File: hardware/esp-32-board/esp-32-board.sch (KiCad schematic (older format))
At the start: 12 parts, among them J1 MainConnector, J2 Conn_01x06, J3 ESP-PROG-Program, J4 ESP-PROG-Debug, SW1 SW_Push, SW2 SW_Push, U1 ESP32-WROOM-32

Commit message: Reannotate schematic
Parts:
- renumbered C3 to C2, C4 to C3, C2 to C4, J3 to J1, J1 to J2, J4 to J3, J2 to J4
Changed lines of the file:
@@
 $EndComp
 $Comp
-L Device:C C3
+L Device:C C2
 U 1 1 5FAC9D96
 P 4850 2950
-F 0 "C3" V 4700 3000 50  0000 L CNN
+F 0 "C2" V 4700 3000 50  0000 L CNN
 F 1 "100nF" V 4700 2650 50  0000 L CNN
 F 2 "Capacitor_SMD:C_0805_2012Metric_Pad1.18x1.45mm_HandSolder" H 4888 2800 50  0001 C CNN
@@
 $EndComp
 $Comp
-L Device:C C4
+L Device:C C3
 U 1 1 5FACA76A
 P 4850 4250
-F 0 "C4" V 4700 4300 50  0000 L CNN
+F 0 "C3" V 4700 4300 50  0000 L CNN
 F 1 "100nF" V 4700 3950 50  0000 L CNN
 F 2 "Capacitor_SMD:C_0805_2012Metric_Pad1.18x1.45mm_HandSolder" H 4888 4100 50  0001 C CNN
@@
 $EndComp
 $Comp
-L Device:C C2
+L Device:C C4
 U 1 1 5FACAC23
 P 5000 1550
-F 0 "C2" H 5050 1650 50  0000 L CNN
+F 0 "C4" H 5050 1650 50  0000 L CNN
 F 1 "100nF" H 5100 1450 50  0000 L CNN
 F 2 "Capacitor_SMD:C_0805_2012Metric_Pad1.18x1.45mm_HandSolder" H 5038 1400 50  0001 C CNN
@@
 	7400 2400 6850 2400
 $Comp
-L Connector:ESP-PROG-Program J3
+L Connector:ESP-PROG-Program J1
 U 1 1 5FECB5F0
 P 7100 5600
-F 0 "J3" H 6700 6100 50  0000 L CNN
+F 0 "J1" H 6700 6100 50  0000 L CNN
 F 1 "ESP-PROG-Program" H 7250 6100 50  0000 L CNN
 F 2 "Connector_IDC:IDC-Header_2x03_P1.27mm_Vertical_SMD" V 6850 5650 50  0001 C CNN
@@
 	7000 6000 7000 6150
 $Comp
-L Connector:ESP-PROG-Debug J4
+L Connector:ESP-PROG-Debug J3
 U 1 1 5FF13734
 P 9100 5600
-F 0 "J4" H 8750 6100 50  0000 R CNN
+F 0 "J3" H 8750 6100 50  0000 R CNN
 F 1 "ESP-PROG-Debug" H 9850 6100 50  0000 R CNN
 F 2 "Connector_IDC:IDC-Header_2x05_P1.27mm_Vertical_SMD" V 8850 5650 50  0001 C CNN
@@
 	9500 5500 9800 5500
 $Comp
-L project_components:MainConnector J1
+L project_components:MainConnector J2
 U 1 1 600797C7
 P 7800 2550
-F 0 "J1" H 7800 3700 50  0000 C CNN
+F 0 "J2" H 7800 3700 50  0000 C CNN
 F 1 "MainConnector" H 7800 3600 50  0000 C CNN
 F 2 "project_components:MainConnector" H 7600 2050 50  0001 C CNN
@@
 	6700 2000 7400 2000
 $Comp
-L Connector_Generic:Conn_01x06 J2
+L Connector_Generic:Conn_01x06 J4
 U 1 1 602A25F3
 P 10000 2450
-F 0 "J2" H 10000 2800 50  0000 C CNN
+F 0 "J4" H 10000 2800 50  0000 C CNN
 F 1 "Conn_01x06" H 10000 2000 50  0000 C CNN
 F 2 "Connector_PinSocket_2.54mm:PinSocket_1x06_P2.54mm_Vertical" H 10000 2450 50  0001 C CNN
@@
 	5000 6100 5000 6700
 $Comp
-L power:PWR_FLAG #FLG0103
+L power:PWR_FLAG #FLG01
 U 1 1 5FD0B643
 P 6600 2000
-F 0 "#FLG0103" H 6600 2075 50  0001 C CNN
+F 0 "#FLG01" H 6600 2075 50  0001 C CNN
 F 1 "PWR_FLAG" V 6600 2150 50  0000 L CNN
 F 2 "" H 6600 2000 50  0001 C CNN
@@
 $EndComp
 $Comp
-L power:+5V #PWR0102
+L power:+5V #PWR015
 U 1 1 5FFB2CC9
 P 8900 1600
-F 0 "#PWR0102" H 8900 1450 50  0001 C CNN
+F 0 "#PWR015" H 8900 1450 50  0001 C CNN
 F 1 "+5V" H 8950 1800 50  0000 C CNN
 F 2 "" H 8900 1600 50  0001 C CNN

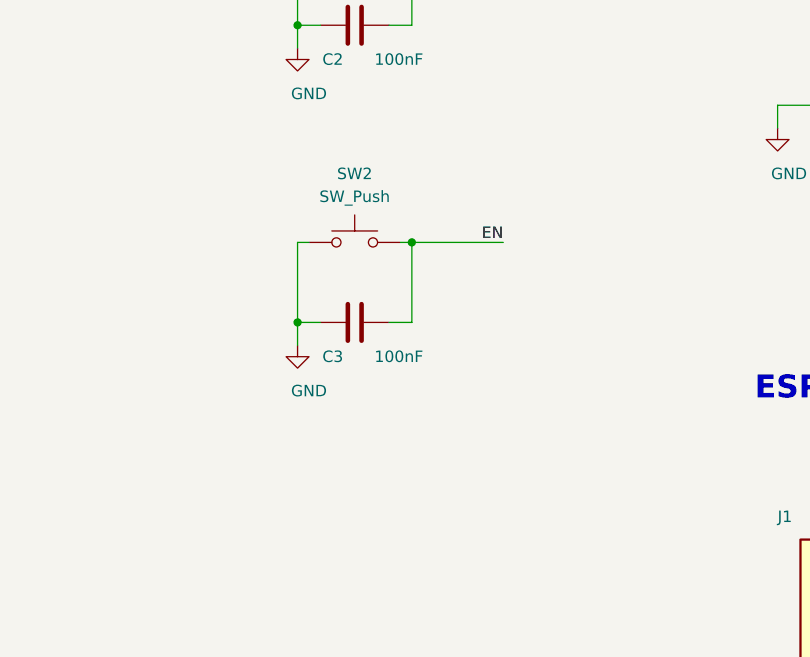
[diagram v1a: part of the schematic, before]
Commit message: Add pullup resistor for EN
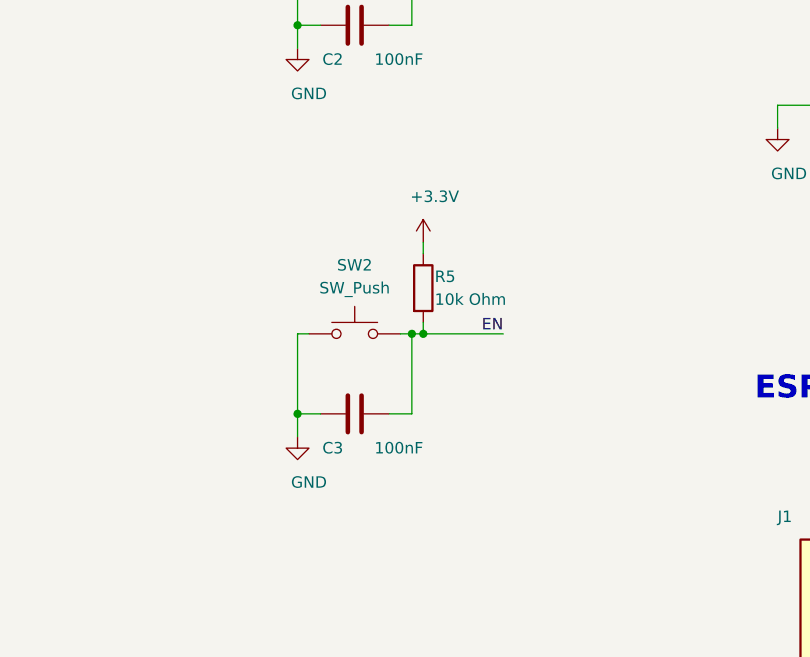
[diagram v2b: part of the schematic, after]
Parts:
- added R5: 10k Ohm, Resistor_SMD:R_0805_2012Metric_Pad1.20x1.40mm_HandSolder, symbol Device:R
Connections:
- wire segments 133 -> 136
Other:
- moved on the sheet: C3, SW2
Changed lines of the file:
@@
 L Device:C C3
 U 1 1 5FACA76A
-P 4850 4250
-F 0 "C3" V 4700 4300 50  0000 L CNN
-F 1 "100nF" V 4700 3950 50  0000 L CNN
-F 2 "Capacitor_SMD:C_0805_2012Metric_Pad1.18x1.45mm_HandSolder" H 4888 4100 50  0001 C CNN
-F 3 "~" H 4850 4250 50  0001 C CNN
-F 4 "avt.pl" H 4850 4250 50  0001 C CNN "Vendor"
-F 5 "https://sklep.avt.pl/zestaw-kondensatorow-smd-0805-720-sztuk.html" H 4850 4250 50  0001 C CNN "VendorLink"
-	1    4850 4250
+P 4850 4650
+F 0 "C3" V 4700 4700 50  0000 L CNN
+F 1 "100nF" V 4700 4350 50  0000 L CNN
+F 2 "Capacitor_SMD:C_0805_2012Metric_Pad1.18x1.45mm_HandSolder" H 4888 4500 50  0001 C CNN
+F 3 "~" H 4850 4650 50  0001 C CNN
+F 4 "avt.pl" H 4850 4650 50  0001 C CNN "Vendor"
+F 5 "https://sklep.avt.pl/zestaw-kondensatorow-smd-0805-720-sztuk.html" H 4850 4650 50  0001 C CNN "VendorLink"
+	1    4850 4650
 	0    -1   -1   0
 $EndComp
@@
 L Switch:SW_Push SW2
 U 1 1 5FB585EB
-P 4850 3900
-F 0 "SW2" H 4850 4200 50  0000 C CNN
-F 1 "SW_Push" H 4850 4100 50  0000 C CNN
-F 2 "Button_Switch_SMD:SW_Push_1P1T_NO_6x6mm_H4.3mm" H 4850 4100 50  0001 C CNN
-F 3 "~" H 4850 4100 50  0001 C CNN
-F 4 "tme.eu" H 4850 3900 50  0001 C CNN "Vendor"
-F 5 "https://www.tme.eu/pl/details/tactm-64n-f/mikroprzelaczniki-tact/ninigi/" H 4850 3900 50  0001 C CNN "VendorLink"
-	1    4850 3900
-	1    0    0    -1
-$EndComp
-Wire Wire Line
-	4650 3900 4600 3900
-Wire Wire Line
-	4600 3900 4600 4250
-Wire Wire Line
-	4700 4250 4600 4250
-Connection ~ 4600 4250
-Wire Wire Line
-	4600 4250 4600 4350
-Wire Wire Line
-	5000 4250 5100 4250
-Wire Wire Line
-	5100 4250 5100 3900
-Wire Wire Line
-	5100 3900 5050 3900
-Wire Wire Line
-	5100 3900 5500 3900
-Connection ~ 5100 3900
+P 4850 4300
+F 0 "SW2" H 4850 4600 50  0000 C CNN
+F 1 "SW_Push" H 4850 4500 50  0000 C CNN
+F 2 "Button_Switch_SMD:SW_Push_1P1T_NO_6x6mm_H4.3mm" H 4850 4500 50  0001 C CNN
+F 3 "~" H 4850 4500 50  0001 C CNN
+F 4 "tme.eu" H 4850 4300 50  0001 C CNN "Vendor"
+F 5 "https://www.tme.eu/pl/details/tactm-64n-f/mikroprzelaczniki-tact/ninigi/" H 4850 4300 50  0001 C CNN "VendorLink"
+	1    4850 4300
+	1    0    0    -1
+$EndComp
+Wire Wire Line
+	4650 4300 4600 4300
+Wire Wire Line
+	4600 4300 4600 4650
+Wire Wire Line
+	4700 4650 4600 4650
+Connection ~ 4600 4650
+Wire Wire Line
+	4600 4650 4600 4750
+Wire Wire Line
+	5000 4650 5100 4650
+Wire Wire Line
+	5100 4650 5100 4300
+Wire Wire Line
+	5100 4300 5050 4300
+Connection ~ 5100 4300
 Wire Wire Line
 	4650 2600 4600 2600
@@
 L power:GND #PWR06
 U 1 1 5FB79E8F
-P 4600 4350
-F 0 "#PWR06" H 4600 4100 50  0001 C CNN
-F 1 "GND" H 4650 4150 50  0000 C CNN
-F 2 "" H 4600 4350 50  0001 C CNN
-F 3 "" H 4600 4350 50  0001 C CNN
-	1    4600 4350
+P 4600 4750
+F 0 "#PWR06" H 4600 4500 50  0001 C CNN
+F 1 "GND" H 4650 4550 50  0000 C CNN
+F 2 "" H 4600 4750 50  0001 C CNN
+F 3 "" H 4600 4750 50  0001 C CNN
+	1    4600 4750
 	1    0    0    -1
 $EndComp
 Text Label 5500 2600 2    50   ~ 0
 IO0
-Text Label 5500 3900 2    50   ~ 0
+Text Label 5500 4300 2    50   ~ 0
 EN
 $Comp
@@
 Wire Wire Line
 	8900 1600 8900 1750
+Wire Wire Line
+	5100 4300 5150 4300
+Wire Wire Line
+	5150 4250 5150 4300
+Wire Wire Line
+	5150 3900 5150 3950
+$Comp
+L Device:R R5
+U 1 1 60021C37
+P 5150 4100
+F 0 "R5" H 5200 4150 50  0000 L CNN
+F 1 "10k Ohm" H 5200 4050 50  0000 L CNN
+F 2 "Resistor_SMD:R_0805_2012Metric_Pad1.20x1.40mm_HandSolder" V 5080 4100 50  0001 C CNN
+F 3 "~" H 5150 4100 50  0001 C CNN
+F 4 "avt.pl" H 5150 4100 50  0001 C CNN "Vendor"
+F 5 "https://sklep.avt.pl/avt701-805.html" H 5150 4100 50  0001 C CNN "VendorLink"
+	1    5150 4100
+	1    0    0    -1
+$EndComp
+$Comp
+L power:+3.3V #PWR026
+U 1 1 60020BE9
+P 5150 3900
+F 0 "#PWR026" H 5150 3750 50  0001 C CNN
+F 1 "+3.3V" H 5200 4100 50  0000 C CNN
+F 2 "" H 5150 3900 50  0001 C CNN
+F 3 "" H 5150 3900 50  0001 C CNN
+	1    5150 3900
+	1    0    0    -1
+$EndComp
+Connection ~ 5150 4300
+Wire Wire Line
+	5150 4300 5500 4300
 $EndSCHEMATC

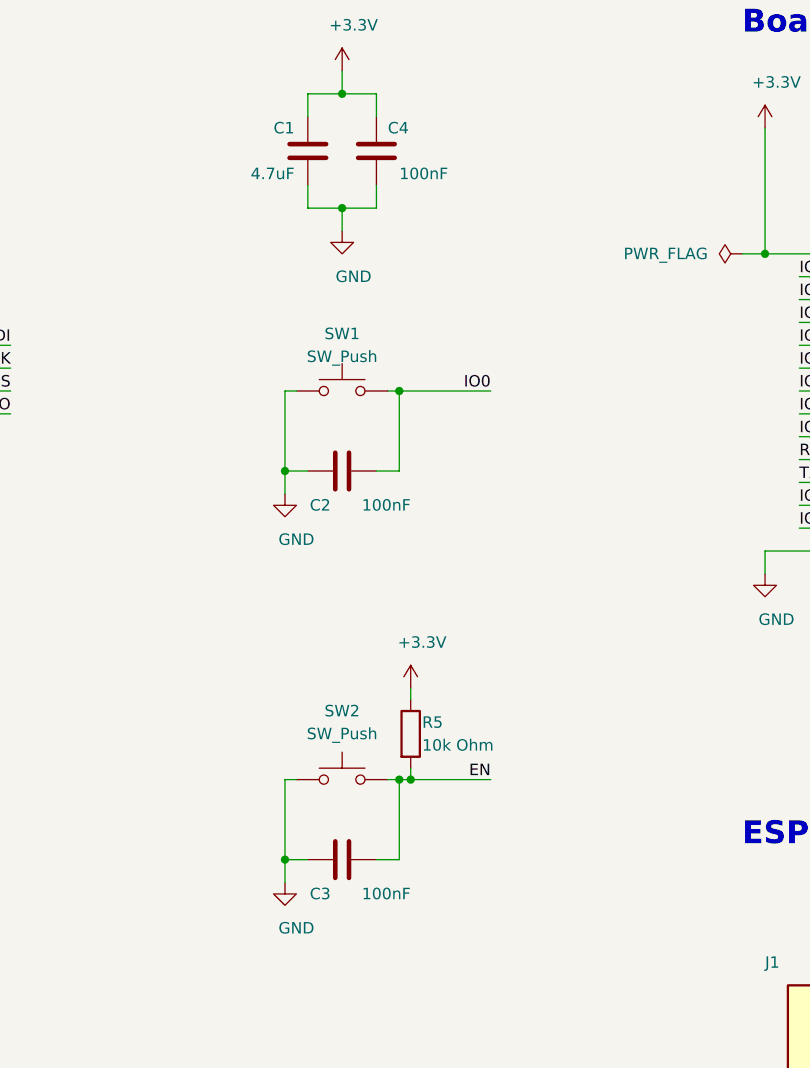
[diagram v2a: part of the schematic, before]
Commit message: Replace Micro USB and button components (no products in stock)
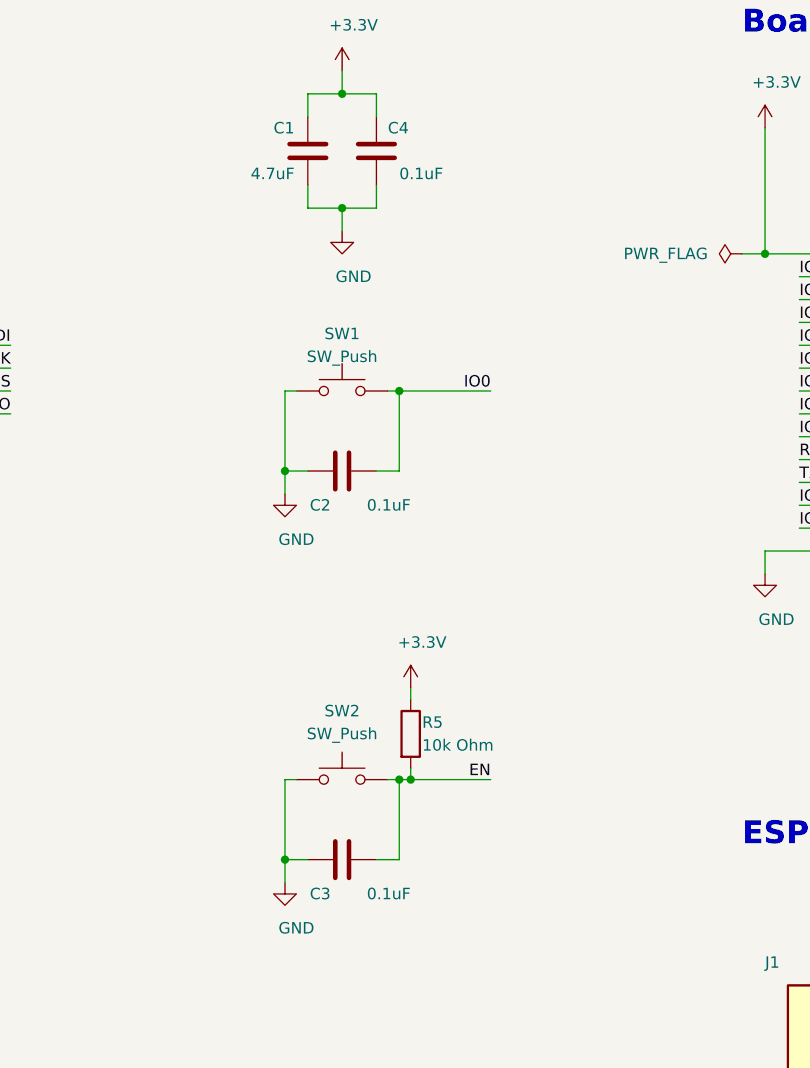
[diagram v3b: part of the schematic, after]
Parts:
- C2, C3, C4: value 100nF -> 0.1uF
- SW1, SW2: VendorLink https://www.tme.eu/pl/details/tactm-64n-f/mikroprzelaczniki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 -> https://www.tme.eu/pl/details/b3s-1000/mikroprzelaczniki-ta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
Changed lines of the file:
@@
 P 4850 2950
 F 0 "C2" V 4700 3000 50  0000 L CNN
-F 1 "100nF" V 4700 2650 50  0000 L CNN
+F 1 "0.1uF" V 4700 2650 50  0000 L CNN
 F 2 "Capacitor_SMD:C_0805_2012Metric_Pad1.18x1.45mm_HandSolder" H 4888 2800 50  0001 C CNN
 F 3 "~" H 4850 2950 50  0001 C CNN
@@
 P 4850 4650
 F 0 "C3" V 4700 4700 50  0000 L CNN
-F 1 "100nF" V 4700 4350 50  0000 L CNN
+F 1 "0.1uF" V 4700 4350 50  0000 L CNN
 F 2 "Capacitor_SMD:C_0805_2012Metric_Pad1.18x1.45mm_HandSolder" H 4888 4500 50  0001 C CNN
 F 3 "~" H 4850 4650 50  0001 C CNN
@@
 P 5000 1550
 F 0 "C4" H 5050 1650 50  0000 L CNN
-F 1 "100nF" H 5100 1450 50  0000 L CNN
+F 1 "0.1uF" H 5100 1450 50  0000 L CNN
 F 2 "Capacitor_SMD:C_0805_2012Metric_Pad1.18x1.45mm_HandSolder" H 5038 1400 50  0001 C CNN
 F 3 "~" H 5000 1550 50  0001 C CNN
@@
 F 1 "SW_Push" H 4850 2750 50  0000 C CNN
 F 2 "Button_Switch_SMD:SW_Push_1P1T_NO_6x6mm_H4.3mm" H 4850 2800 50  0001 C CNN
-F 3 "~" H 4850 2800 50  0001 C CNN
+F 3 "" H 4850 2800 50  0001 C CNN
 F 4 "tme.eu" H 4850 2600 50  0001 C CNN "Vendor"
-F 5 "https://www.tme.eu/pl/details/tactm-64n-f/mikroprzelaczniki-tact/ninigi/" H 4850 2600 50  0001 C CNN "VendorLink"
+F 5 "https://www.tme.eu/pl/details/b3s-1000/mikroprzelaczniki-tact/omron-ocb/" H 4850 2600 50  0001 C CNN "VendorLink"
 	1    4850 2600
 	1    0    0    -1
@@
 F 1 "SW_Push" H 4850 4500 50  0000 C CNN
 F 2 "Button_Switch_SMD:SW_Push_1P1T_NO_6x6mm_H4.3mm" H 4850 4500 50  0001 C CNN
-F 3 "~" H 4850 4500 50  0001 C CNN
+F 3 "" H 4850 4500 50  0001 C CNN
 F 4 "tme.eu" H 4850 4300 50  0001 C CNN "Vendor"
-F 5 "https://www.tme.eu/pl/details/tactm-64n-f/mikroprzelaczniki-tact/ninigi/" H 4850 4300 50  0001 C CNN "VendorLink"
+F 5 "https://www.tme.eu/pl/details/b3s-1000/mikroprzelaczniki-tact/omron-ocb/" H 4850 4300 50  0001 C CNN "VendorLink"
 	1    4850 4300
 	1    0    0    -1
